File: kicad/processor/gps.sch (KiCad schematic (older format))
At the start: 12 parts, among them Q401 DMG3415U, U401 FGPMMOPA6H GPS

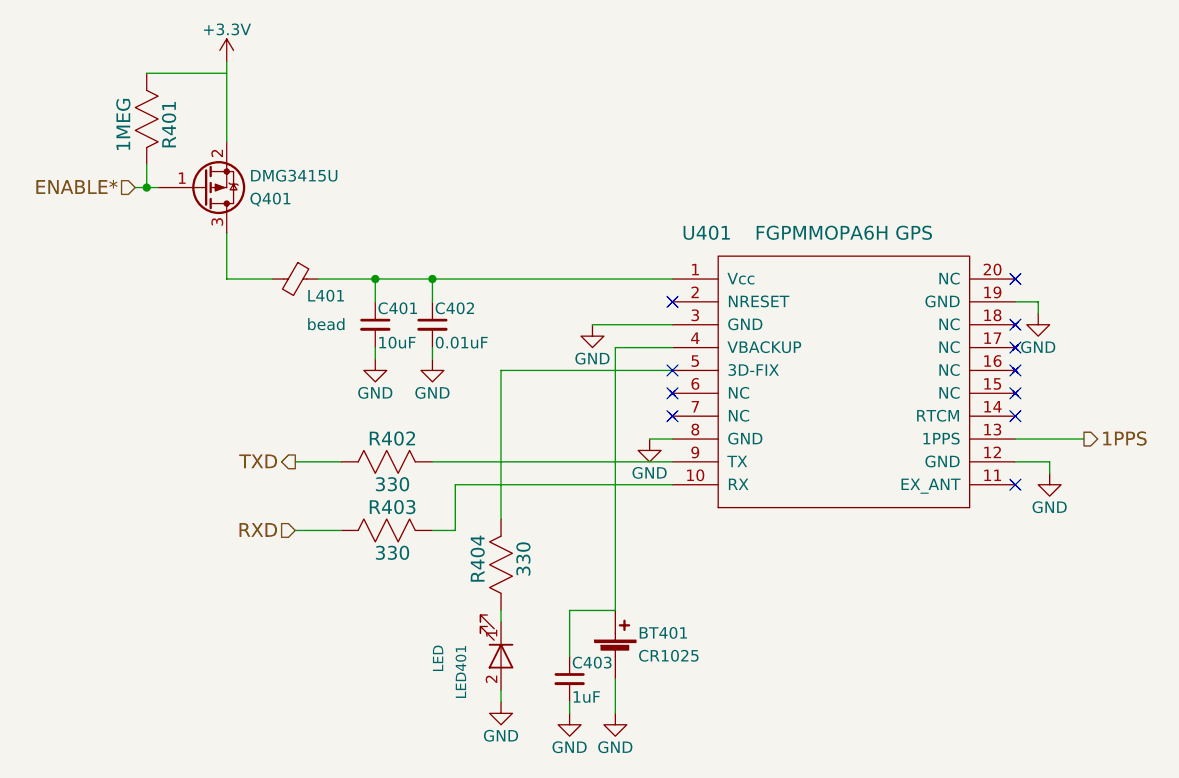
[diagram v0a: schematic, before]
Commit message: Finish split projects, fix ERC, import outline to processor board
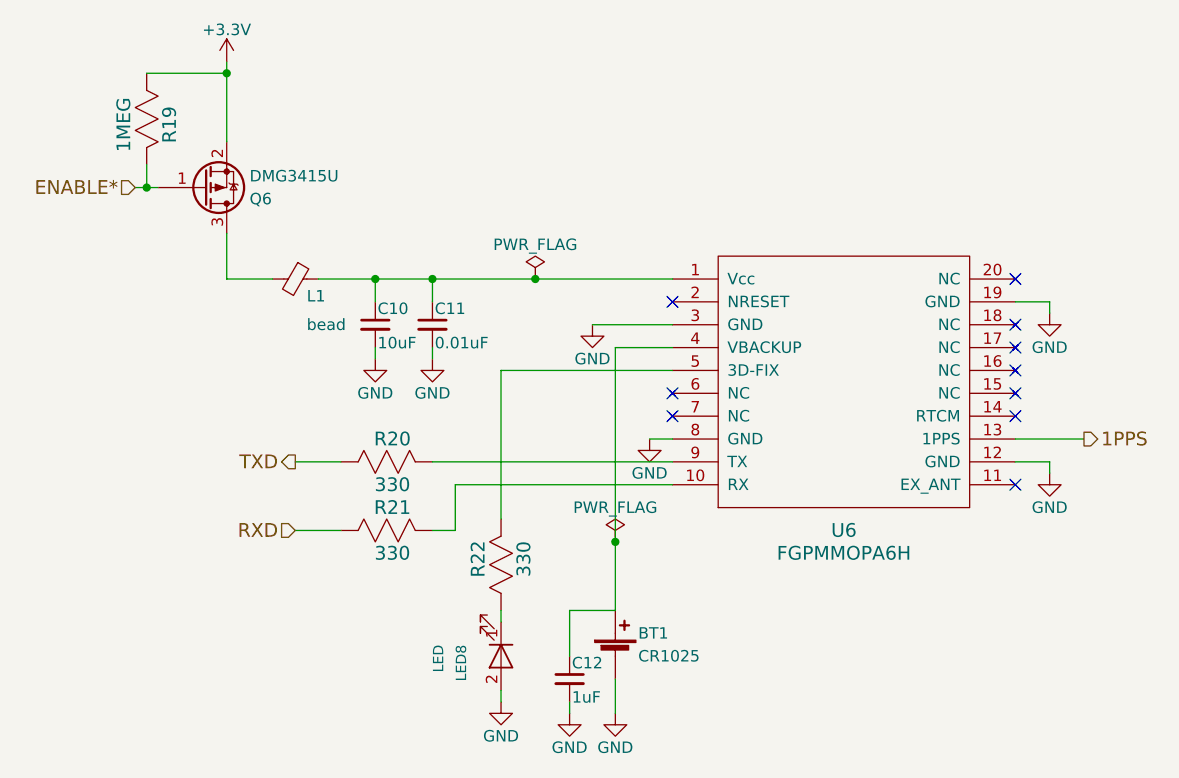
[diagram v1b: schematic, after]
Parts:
- removed U401: FGPMMOPA6H GPS, paddle:FGPMMOPA6H, symbol FGPMMOPA6H
- added U6: FGPMMOPA6H, symbol FGPMMOPA6H
- renumbered BT401 to BT1, C401 to C10, C402 to C11, C403 to C12, L401 to L1, LED401 to LED8, Q401 to Q6, R401 to R19, R402 to R20, R403 to R21, R404 to R22
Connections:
- net +3V3: now also R19.1
- net 1PPS: now also U6.13 (1PPS)
- net GND: now also U6.12 (GND), U6.19 (GND), U6.3 (GND), U6.8 (GND)
- net at C10.1, C11.1, L1.1: now also U6.1 (Vcc)
- net at R21.2: now also U6.10 (RX)
- net at BT1.+, C12.1: now also U6.4 (VBACKUP)
- net at R22.2: now also U6.5 (3D-FIX)
- net at R20.2: now also U6.9 (TX)
- no-connect marks 11 -> 10
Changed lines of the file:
@@
 LIBS:regul
 LIBS:paddle
+LIBS:processor-cache
 EELAYER 25 0
 EELAYER END
@@
 $EndDescr
 $Comp
-L FGPMMOPA6H U401
-U 1 1 59CAA04C
-P 6050 4200
-F 0 "U401" H 5450 4850 60  0000 C CNN
-F 1 "FGPMMOPA6H GPS" H 6050 4850 60  0000 C CNN
-F 2 "paddle:FGPMMOPA6H" H 5725 4100 60  0001 C CNN
-F 3 "" H 5725 4100 60  0001 C CNN
-	1    6050 4200
-	1    0    0    -1
-$EndComp
-$Comp
-L GND #PWR309
-U 1 1 59CAA053
-P 6900 3900
-F 0 "#PWR309" H 6900 3650 50  0001 C CNN
-F 1 "GND" H 6900 3750 50  0000 C CNN
-F 2 "" H 6900 3900 50  0001 C CNN
-F 3 "" H 6900 3900 50  0001 C CNN
-	1    6900 3900
-	1    0    0    -1
-$EndComp
-$Comp
-L GND #PWR310
+L GND #PWR046
 U 1 1 59CAA059
 P 6950 4600
-F 0 "#PWR310" H 6950 4350 50  0001 C CNN
+F 0 "#PWR046" H 6950 4350 50  0001 C CNN
 F 1 "GND" H 6950 4450 50  0000 C CNN
 F 2 "" H 6950 4600 50  0001 C CNN
@@
 NoConn ~ 5300 4250
 NoConn ~ 5300 4350
-NoConn ~ 5300 4150
 NoConn ~ 6800 4350
 NoConn ~ 6800 4650
 $Comp
-L LED LED?
+L LED LED8
 U 1 1 59CAA06A
 P 4550 5400
-AR Path="/59C7A5C1/59CAA06A" Ref="LED?"  Part="1"
-AR Path="/59CAA06A" Ref="LED?"  Part="1"
-AR Path="/59CA9ED7/59CAA06A" Ref="LED401"  Part="1"
-AR Path="/59FFAC69/59CAA06A" Ref="LED401"  Part="1"
-F 0 "LED401" H 4500 5200 45  0000 L BNN
+F 0 "LED8" H 4500 5200 45  0000 L BNN
 F 1 "LED" H 4500 5100 45  0000 L BNN
 F 2 "paddle:SMD_D_0805" H 4350 5430 20  0001 C CNN
@@
 $EndComp
 $Comp
-L R_US R404
+L R_US R22
 U 1 1 59CAA071
 P 4550 5000
-F 0 "R404" H 4575 5100 60  0000 C CNN
+F 0 "R22" H 4575 5100 60  0000 C CNN
 F 1 "330" H 4575 4900 60  0000 C CNN
 F 2 "paddle:SMD_0805" H 4550 4650 60  0001 C CNN
@@
 $EndComp
 $Comp
-L GND #PWR304
+L GND #PWR047
 U 1 1 59CAA078
 P 4550 5600
-F 0 "#PWR304" H 4550 5350 50  0001 C CNN
+F 0 "#PWR047" H 4550 5350 50  0001 C CNN
 F 1 "GND" H 4550 5450 50  0000 C CNN
 F 2 "" H 4550 5600 50  0001 C CNN
@@
 	6950 4600 6950 4550
 Wire Wire Line
-	6900 3850 6900 3900
-Wire Wire Line
-	6800 3850 6900 3850
-Wire Wire Line
 	5200 4450 5300 4450
 Wire Wire Line
@@
 	3350 2800 3350 3150
 $Comp
-L Q_PMOS_GSD Q401
+L Q_PMOS_GSD Q6
 U 1 1 59CAD4AE
 P 3250 3350
-F 0 "Q401" H 3450 3400 50  0000 L CNN
+F 0 "Q6" H 3450 3400 50  0000 L CNN
 F 1 "DMG3415U" H 3450 3300 50  0000 L CNN
 F 2 "paddle:SOT-23" H 3450 3450 50  0001 C CNN
@@
 $EndComp
 $Comp
-L +3.3V #PWR301
+L +3.3V #PWR048
 U 1 1 59CB0B2A
 P 3350 2800
-F 0 "#PWR301" H 3350 2650 50  0001 C CNN
+F 0 "#PWR048" H 3350 2650 50  0001 C CNN
 F 1 "+3.3V" H 3350 2940 50  0000 C CNN
 F 2 "" H 3350 2800 50  0001 C CNN
@@
 $EndComp
 $Comp
-L C_Small C402
+L C_Small C11
 U 1 1 59CB0B30
 P 4250 3950
-F 0 "C402" H 4260 4020 50  0000 L CNN
+F 0 "C11" H 4260 4020 50  0000 L CNN
 F 1 "0.01uF" H 4260 3870 50  0000 L CNN
 F 2 "paddle:SMD_0805" H 4250 3950 50  0001 C CNN
@@
 $EndComp
 $Comp
-L GND #PWR303
+L GND #PWR049
 U 1 1 59CB0B37
 P 4250 4100
-F 0 "#PWR303" H 4250 3850 50  0001 C CNN
+F 0 "#PWR049" H 4250 3850 50  0001 C CNN
 F 1 "GND" H 4250 3950 50  0000 C CNN
 F 2 "" H 4250 4100 50  0001 C CNN
@@
 $EndComp
 $Comp
-L C_Small C401
+L C_Small C10
 U 1 1 59CB0B3D
 P 4000 3950
-F 0 "C401" H 4010 4020 50  0000 L CNN
+F 0 "C10" H 4010 4020 50  0000 L CNN
 F 1 "10uF" H 4010 3870 50  0000 L CNN
 F 2 "paddle:SMD_1206" H 4000 3950 50  0001 C CNN
@@
 $EndComp
 $Comp
-L GND #PWR302
+L GND #PWR050
 U 1 1 59CB0B44
 P 4000 4100
-F 0 "#PWR302" H 4000 3850 50  0001 C CNN
+F 0 "#PWR050" H 4000 3850 50  0001 C CNN
 F 1 "GND" H 4000 3950 50  0000 C CNN
 F 2 "" H 4000 4100 50  0001 C CNN
@@
 	2950 3350 3050 3350
 $Comp
-L R_US R401
+L R_US R19
 U 1 1 59CB0CA3
 P 3000 3050
-F 0 "R401" H 3025 3150 60  0000 C CNN
+F 0 "R19" H 3025 3150 60  0000 C CNN
 F 1 "1MEG" H 3025 2950 60  0000 C CNN
 F 2 "paddle:SMD_0805" H 3000 2700 60  0001 C CNN
@@
 TXD
 $Comp
-L GND #PWR306
+L GND #PWR051
 U 1 1 59CB0DB1
 P 4950 3950
-F 0 "#PWR306" H 4950 3700 50  0001 C CNN
+F 0 "#PWR051" H 4950 3700 50  0001 C CNN
 F 1 "GND" H 4950 3800 50  0000 C CNN
 F 2 "" H 4950 3950 50  0001 C CNN
@@
 $EndComp
 $Comp
-L GND #PWR308
+L GND #PWR052
 U 1 1 59CB12C3
 P 5200 4450
-F 0 "#PWR308" H 5200 4200 50  0001 C CNN
+F 0 "#PWR052" H 5200 4200 50  0001 C CNN
 F 1 "GND" H 5200 4300 50  0000 C CNN
 F 2 "" H 5200 4450 50  0001 C CNN
@@
 $EndComp
 $Comp
-L GND #PWR307
+L GND #PWR053
 U 1 1 59CB3240
 P 5050 5650
-F 0 "#PWR307" H 5050 5400 50  0001 C CNN
+F 0 "#PWR053" H 5050 5400 50  0001 C CNN
 F 1 "GND" H 5050 5500 50  0000 C CNN
 F 2 "" H 5050 5650 50  0001 C CNN
@@
 	5050 4050 5050 5200
 $Comp
-L C_Small C403
+L C_Small C12
 U 1 1 59CB3249
 P 4850 5500
-F 0 "C403" H 4860 5570 50  0000 L CNN
+F 0 "C12" H 4860 5570 50  0000 L CNN
 F 1 "1uF" H 4860 5420 50  0000 L CNN
 F 2 "paddle:SMD_0805" H 4850 5500 50  0001 C CNN
@@
 $EndComp
 $Comp
-L GND #PWR305
+L GND #PWR054
 U 1 1 59CB3250
 P 4850 5650
-F 0 "#PWR305" H 4850 5400 50  0001 C CNN
+F 0 "#PWR054" H 4850 5400 50  0001 C CNN
 F 1 "GND" H 4850 5500 50  0000 C CNN
 F 2 "" H 4850 5650 50  0001 C CNN
@@
 	5050 5200 4850 5200
 $Comp
-L R_US R402
+L R_US R20
 U 1 1 59CB67E4
 P 4050 4550
-F 0 "R402" H 4075 4650 60  0000 C CNN
+F 0 "R20" H 4075 4650 60  0000 C CNN
 F 1 "330" H 4075 4450 60  0000 C CNN
 F 2 "paddle:SMD_0805" H 4050 4200 60  0001 C CNN
@@
 $EndComp
 $Comp
-L R_US R403
+L R_US R21
 U 1 1 59CB67EB
 P 4050 4850
-F 0 "R403" H 4075 4950 60  0000 C CNN
+F 0 "R21" H 4075 4950 60  0000 C CNN
 F 1 "330" H 4075 4750 60  0000 C CNN
 F 2 "paddle:SMD_0805" H 4050 4500 60  0001 C CNN
@@
 	4350 4650 5300 4650
 $Comp
-L Ferrite_Bead_Small L401
+L Ferrite_Bead_Small L1
 U 1 1 59CB7059
 P 3650 3750
-F 0 "L401" V 3725 3800 50  0000 L CNN
+F 0 "L1" V 3725 3800 50  0000 L CNN
 F 1 "bead" V 3850 3800 50  0000 L CNN
 F 2 "paddle:SMD_0805" V 3580 3750 50  0001 C CNN
@@
 	3750 3750 5300 3750
 $Comp
-L Battery_single-cell BT401
+L Battery_single-cell BT1
 U 1 1 59D0200B
 P 5050 5400
-F 0 "BT401" H 5150 5500 50  0000 L CNN
+F 0 "BT1" H 5150 5500 50  0000 L CNN
 F 1 "CR1025" H 5150 5400 50  0000 L CNN
 F 2 "paddle:CR1025_holder" V 5050 5460 50  0001 C CNN
@@
 $EndComp
 NoConn ~ 5300 3850
+$Comp
+L FGPMMOPA6H U6
+U 1 1 5A055330
+P 6050 4200
+F 0 "U6" H 6050 3550 60  0000 C CNN
+F 1 "FGPMMOPA6H" H 6050 3450 60  0000 C CNN
+F 2 "" H 5725 4100 60  0001 C CNN
+F 3 "" H 5725 4100 60  0001 C CNN
+	1    6050 4200
+	1    0    0    -1
+$EndComp
+$Comp
+L GND #PWR055
+U 1 1 59FFEC60
+P 6950 3900
+F 0 "#PWR055" H 6950 3650 50  0001 C CNN
+F 1 "GND" H 6950 3750 50  0000 C CNN
+F 2 "" H 6950 3900 50  0001 C CNN
+F 3 "" H 6950 3900 50  0001 C CNN
+	1    6950 3900
+	1    0    0    -1
+$EndComp
+Wire Wire Line
+	6950 3900 6950 3850
+Wire Wire Line
+	6950 3850 6800 3850
+Connection ~ 3350 2850
+$Comp
+L PWR_FLAG #FLG056
+U 1 1 59FFC967
+P 4700 3750
+F 0 "#FLG056" H 4700 3825 50  0001 C CNN
+F 1 "PWR_FLAG" H 4700 3900 50  0000 C CNN
+F 2 "" H 4700 3750 50  0001 C CNN
+F 3 "" H 4700 3750 50  0001 C CNN
+	1    4700 3750
+	1    0    0    -1
+$EndComp
+Connection ~ 4700 3750
+$Comp
+L PWR_FLAG #FLG057
+U 1 1 59FFCDE5
+P 5050 4900
+F 0 "#FLG057" H 5050 4975 50  0001 C CNN
+F 1 "PWR_FLAG" H 5050 5050 50  0000 C CNN
+F 2 "" H 5050 4900 50  0001 C CNN
+F 3 "" H 5050 4900 50  0001 C CNN
+	1    5050 4900
+	1    0    0    -1
+$EndComp
+Connection ~ 5050 4900
 $EndSCHEMATC

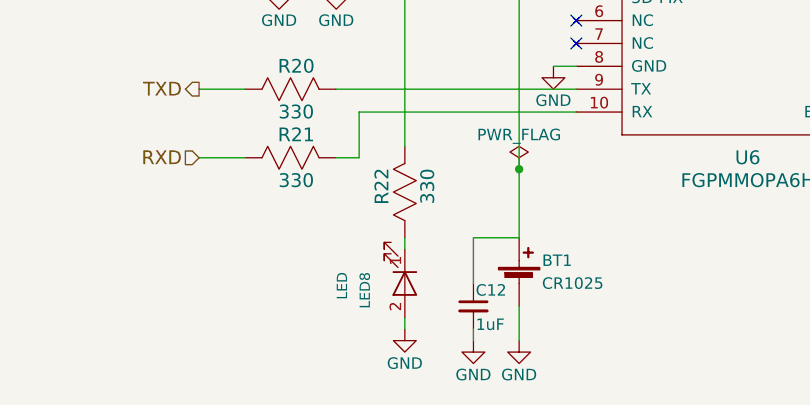
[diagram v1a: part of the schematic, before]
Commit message: Logic board standalone about done, changed to 0603 resistors and 0805 caps
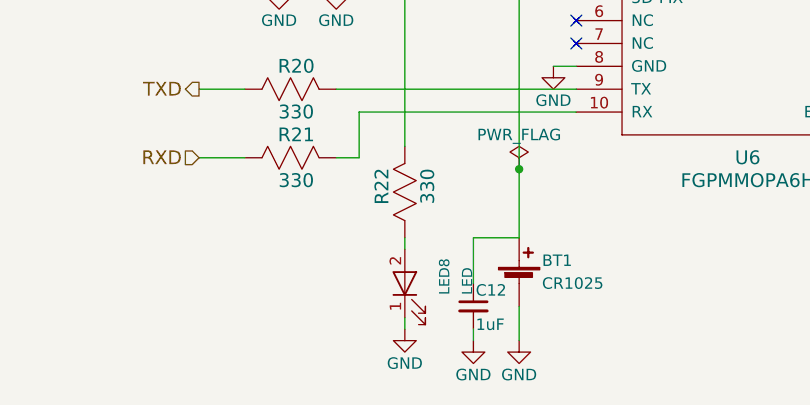
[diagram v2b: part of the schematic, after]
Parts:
- C10: footprint paddle:SMD_1206 -> paddle:SMD_0805
- R19, R20, R21, R22: footprint paddle:SMD_0805 -> paddle:R_0603
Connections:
- net GND: now also LED8.1 (K); no longer LED8.2 (A)
- net at R22.1: now also LED8.2 (A); no longer LED8.1 (K)
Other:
- moved on the sheet: LED8
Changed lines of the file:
@@
 F 3 "" V 4500 5400 60  0001 C CNN
 	1    4550 5400
-	0    1    1    0
+	0    -1   -1   0
 $EndComp
 $Comp
@@
 F 0 "R22" H 4575 5100 60  0000 C CNN
 F 1 "330" H 4575 4900 60  0000 C CNN
-F 2 "paddle:SMD_0805" H 4550 4650 60  0001 C CNN
+F 2 "paddle:R_0603" H 4550 4650 60  0001 C CNN
 F 3 "" H 4575 5100 60  0000 C CNN
 	1    4550 5000
@@
 F 0 "C10" H 4010 4020 50  0000 L CNN
 F 1 "10uF" H 4010 3870 50  0000 L CNN
-F 2 "paddle:SMD_1206" H 4000 3950 50  0001 C CNN
+F 2 "paddle:SMD_0805" H 4000 3950 50  0001 C CNN
 F 3 "" H 4000 3950 50  0001 C CNN
 	1    4000 3950
@@
 F 0 "R19" H 3025 3150 60  0000 C CNN
 F 1 "1MEG" H 3025 2950 60  0000 C CNN
-F 2 "paddle:SMD_0805" H 3000 2700 60  0001 C CNN
+F 2 "paddle:R_0603" H 3000 2700 60  0001 C CNN
 F 3 "" H 3025 3150 60  0000 C CNN
 	1    3000 3050
@@
 F 0 "R20" H 4075 4650 60  0000 C CNN
 F 1 "330" H 4075 4450 60  0000 C CNN
-F 2 "paddle:SMD_0805" H 4050 4200 60  0001 C CNN
+F 2 "paddle:R_0603" H 4050 4200 60  0001 C CNN
 F 3 "" H 4075 4650 60  0000 C CNN
 	1    4050 4550
@@
 F 0 "R21" H 4075 4950 60  0000 C CNN
 F 1 "330" H 4075 4750 60  0000 C CNN
-F 2 "paddle:SMD_0805" H 4050 4500 60  0001 C CNN
+F 2 "paddle:R_0603" H 4050 4500 60  0001 C CNN
 F 3 "" H 4075 4950 60  0000 C CNN
 	1    4050 4850

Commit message: start processor layout - footprint fixes
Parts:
- U6: footprint (none) -> paddle:FGPMMOPA6H
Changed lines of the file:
@@
 F 0 "U6" H 6050 3550 60  0000 C CNN
 F 1 "FGPMMOPA6H" H 6050 3450 60  0000 C CNN
-F 2 "" H 5725 4100 60  0001 C CNN
+F 2 "paddle:FGPMMOPA6H" H 5725 4100 60  0001 C CNN
 F 3 "" H 5725 4100 60  0001 C CNN
 	1    6050 4200

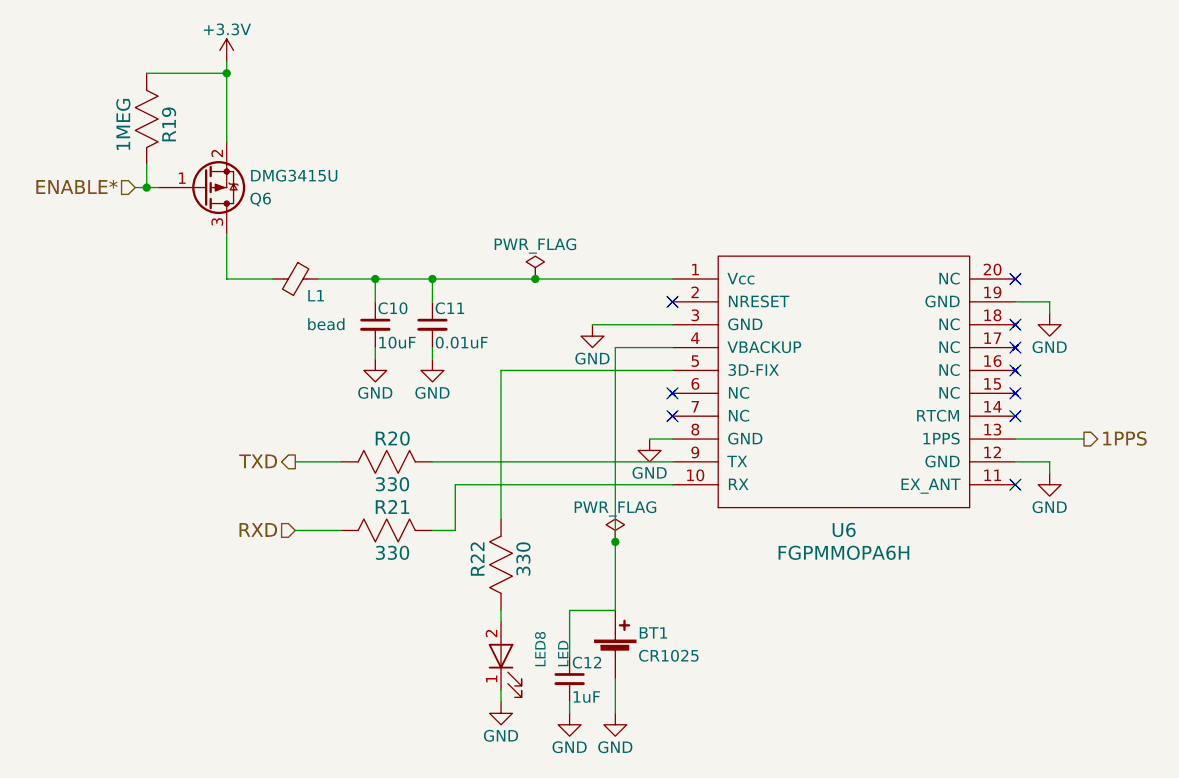
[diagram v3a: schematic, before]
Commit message: First cut layout power supply, fix netclasses, footprint for connector
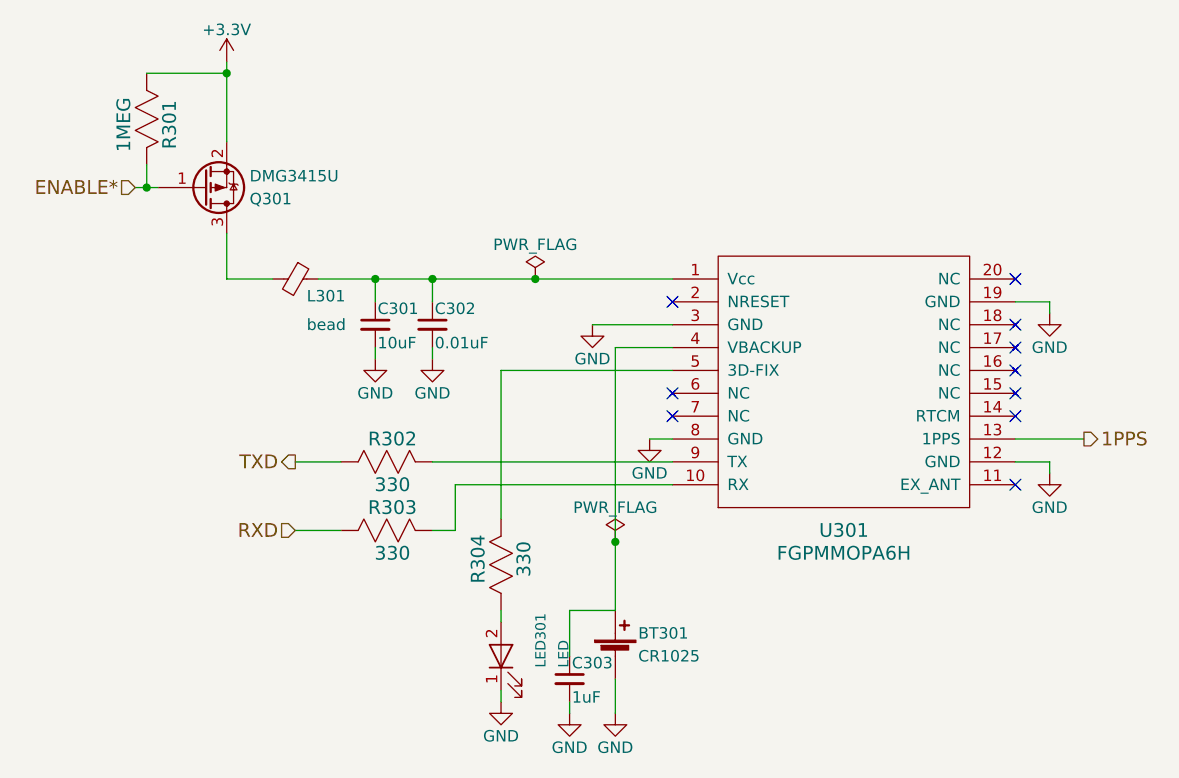
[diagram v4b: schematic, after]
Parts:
- renumbered BT1 to BT301, C10 to C301, C11 to C302, C12 to C303, L1 to L301, LED8 to LED301, Q6 to Q301, R19 to R301, R20 to R302, R21 to R303, R22 to R304, U6 to U301
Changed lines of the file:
@@
 NoConn ~ 6800 4650
 $Comp
-L LED LED8
+L LED LED301
 U 1 1 59CAA06A
 P 4550 5400
-F 0 "LED8" H 4500 5200 45  0000 L BNN
+F 0 "LED301" H 4500 5200 45  0000 L BNN
 F 1 "LED" H 4500 5100 45  0000 L BNN
 F 2 "paddle:SMD_D_0805" H 4350 5430 20  0001 C CNN
@@
 $EndComp
 $Comp
-L R_US R22
+L R_US R304
 U 1 1 59CAA071
 P 4550 5000
-F 0 "R22" H 4575 5100 60  0000 C CNN
+F 0 "R304" H 4575 5100 60  0000 C CNN
 F 1 "330" H 4575 4900 60  0000 C CNN
 F 2 "paddle:R_0603" H 4550 4650 60  0001 C CNN
@@
 	3350 2800 3350 3150
 $Comp
-L Q_PMOS_GSD Q6
+L Q_PMOS_GSD Q301
 U 1 1 59CAD4AE
 P 3250 3350
-F 0 "Q6" H 3450 3400 50  0000 L CNN
+F 0 "Q301" H 3450 3400 50  0000 L CNN
 F 1 "DMG3415U" H 3450 3300 50  0000 L CNN
 F 2 "paddle:SOT-23" H 3450 3450 50  0001 C CNN
@@
 $EndComp
 $Comp
-L C_Small C11
+L C_Small C302
 U 1 1 59CB0B30
 P 4250 3950
-F 0 "C11" H 4260 4020 50  0000 L CNN
+F 0 "C302" H 4260 4020 50  0000 L CNN
 F 1 "0.01uF" H 4260 3870 50  0000 L CNN
 F 2 "paddle:SMD_0805" H 4250 3950 50  0001 C CNN
@@
 $EndComp
 $Comp
-L C_Small C10
+L C_Small C301
 U 1 1 59CB0B3D
 P 4000 3950
-F 0 "C10" H 4010 4020 50  0000 L CNN
+F 0 "C301" H 4010 4020 50  0000 L CNN
 F 1 "10uF" H 4010 3870 50  0000 L CNN
 F 2 "paddle:SMD_0805" H 4000 3950 50  0001 C CNN
@@
 	2950 3350 3050 3350
 $Comp
-L R_US R19
+L R_US R301
 U 1 1 59CB0CA3
 P 3000 3050
-F 0 "R19" H 3025 3150 60  0000 C CNN
+F 0 "R301" H 3025 3150 60  0000 C CNN
 F 1 "1MEG" H 3025 2950 60  0000 C CNN
 F 2 "paddle:R_0603" H 3000 2700 60  0001 C CNN
@@
 	5050 4050 5050 5200
 $Comp
-L C_Small C12
+L C_Small C303
 U 1 1 59CB3249
 P 4850 5500
-F 0 "C12" H 4860 5570 50  0000 L CNN
+F 0 "C303" H 4860 5570 50  0000 L CNN
 F 1 "1uF" H 4860 5420 50  0000 L CNN
 F 2 "paddle:SMD_0805" H 4850 5500 50  0001 C CNN
@@
 	5050 5200 4850 5200
 $Comp
-L R_US R20
+L R_US R302
 U 1 1 59CB67E4
 P 4050 4550
-F 0 "R20" H 4075 4650 60  0000 C CNN
+F 0 "R302" H 4075 4650 60  0000 C CNN
 F 1 "330" H 4075 4450 60  0000 C CNN
 F 2 "paddle:R_0603" H 4050 4200 60  0001 C CNN
@@
 $EndComp
 $Comp
-L R_US R21
+L R_US R303
 U 1 1 59CB67EB
 P 4050 4850
-F 0 "R21" H 4075 4950 60  0000 C CNN
+F 0 "R303" H 4075 4950 60  0000 C CNN
 F 1 "330" H 4075 4750 60  0000 C CNN
 F 2 "paddle:R_0603" H 4050 4500 60  0001 C CNN
@@
 	4350 4650 5300 4650
 $Comp
-L Ferrite_Bead_Small L1
+L Ferrite_Bead_Small L301
 U 1 1 59CB7059
 P 3650 3750
-F 0 "L1" V 3725 3800 50  0000 L CNN
+F 0 "L301" V 3725 3800 50  0000 L CNN
 F 1 "bead" V 3850 3800 50  0000 L CNN
 F 2 "paddle:SMD_0805" V 3580 3750 50  0001 C CNN
@@
 	3750 3750 5300 3750
 $Comp
-L Battery_single-cell BT1
+L Battery_single-cell BT301
 U 1 1 59D0200B
 P 5050 5400
-F 0 "BT1" H 5150 5500 50  0000 L CNN
+F 0 "BT301" H 5150 5500 50  0000 L CNN
 F 1 "CR1025" H 5150 5400 50  0000 L CNN
 F 2 "paddle:CR1025_holder" V 5050 5460 50  0001 C CNN
@@
 NoConn ~ 5300 3850
 $Comp
-L FGPMMOPA6H U6
+L FGPMMOPA6H U301
 U 1 1 5A055330
 P 6050 4200
-F 0 "U6" H 6050 3550 60  0000 C CNN
+F 0 "U301" H 6050 3550 60  0000 C CNN
 F 1 "FGPMMOPA6H" H 6050 3450 60  0000 C CNN
 F 2 "paddle:FGPMMOPA6H" H 5725 4100 60  0001 C CNN
